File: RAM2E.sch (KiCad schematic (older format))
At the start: 19 parts, among them J1 AppleIIeAux, U1 EPM7128SL84, U2 2M x 8

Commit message: halfway done widening clearances
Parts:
- removed U2: 2M x 8, stdpads:SOJ-28-300mil, symbol Connector_Generic:Conn_02x14_Counter_Clockwise
- added C9: 10p, stdpads:C_0805, symbol Device:C_Small
- added R1: 820, stdpads:R_0805, symbol Device:R_Small
- added U2: DRAM_2Mx8, stdpads:SOJ-28-300mil, symbol stdparts:DRAM_2Mx8
- FID1, FID2, FID3, FID4: symbol Mechanical:MountingHole -> Mechanical:Fiducial
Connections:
- wire segments 260 -> 265
- no-connect marks 4 -> 5
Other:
- note added: "= don’t care"
- note added: "State = { PHI0, C7M, nPRAS, nPCAS, Q3 }\nGateCRAS <= state == 10100 | 01111 | 00011 | 01011 @ C14M↑\nnRefRAS <= ~state == 01111 | 01011 | 00001~ @ C14M↑\nnRefCAS <= ~state == 01111 | 00011~ @ C14M↓\nGateWE <= state == 10100 | 00011 @ C14M↑\nHoldRow <= state == 01011 | 10011 @ C14M↓\n\nRowAddr[7:0] <= MA[7:0] @ nPRAS↓\nBA[5:0] <= (state==10100 & RowAddr==73 & C07X) ? D[5:0] : BA[5:0] @ C14M↑"
- note added: "nRAS <= GateCRAS ? nRefRAS : nPRAS\nnCAS <= GateCRAS ? nRefCAS : Q3\nnRWE <= GateWE | RW80\nRA[7:0] <= HoldRow ? RowAddr[7:0] : MA[7:0]\nRA[10:8] <= PHI1 ? 0 : HoldRow ? BA[5:3] : BA[2:0]\nRA[11] <= PHI1 ? 0 : BA[5]\n\nVDR[7:0] <= RD[7:0] @ PHI0\nVD[7:0] <= PHI1 ? 8’bZ : VDR[7:0]\nD[7:0] <= (EN80 & R~W~80) ? RD[7:0] : 8’bZ\nRD[7:0] <= (EN80 & ~R~W80) ? D[7:0] : 8’bZ"
- note removed: "GateCRAS <= state == 10100 | 01111 | 00011 | 01011 @ C14M\nnRefRAS <= ~state == 01111 | 01011 | 00001~ @ C14M\nnRefCAS <= ~state == 01111 | 00011~ @ ~C14M~\nGateWE <= state == 10100 | 00011 @ C14M\nHoldRow <= state == 01011 | 10011 @ ~C14M~\n\nRowAddr[7:0] <= MA[7:0] @ ~nPRAS~\nBA[5:0] <= D[5:0] @ C14M in state == 10100 & RowAddr == 73 & C07X"
- note removed: "VDR[7:0] <= RD[7:0] @ PHI0\nVD[7:0] <= PHI1 ? 8’bZ : VDR[7:0]\nD[7:0] <= (EN80 & R~W~80) ? RD[7:0] : 8’bZ\nRD[7:0] <= (EN80 & ~R~W80) ? D[7:0] : 8’bZ"
- note removed: "nRAS <= GateCRAS ? nRefRAS : nPRAS\nnCAS <= GateCRAS ? nRefCAS : Q3\nnRWE <= GateWE | RW80\nRA[7:0] <= HoldRow ? RowAddr[7:0] : MA[7:0]\nRA[10:8] <= PHI1 ? 0 : HoldRow ? BA[5:3] : BA[2:0]\nRA[11] <= PHI1 ? 0 : BA[5]"
- moved on the sheet: C1, C2, C3, C4, C5, C6, C7, C8, H1, H2, H3, H4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

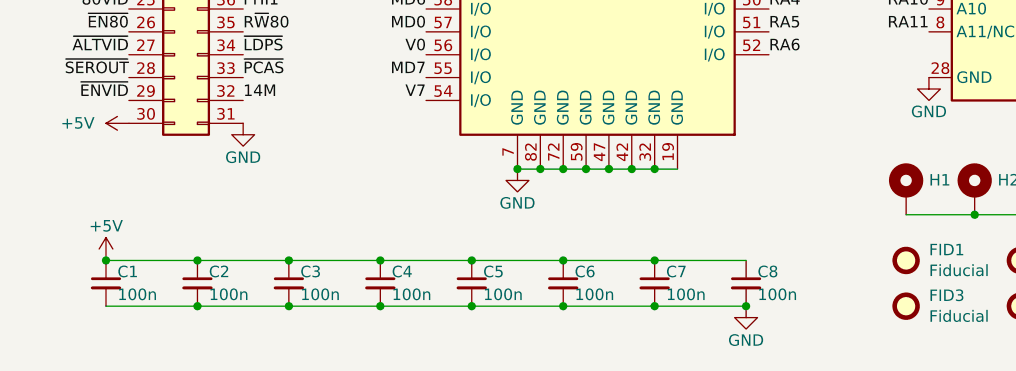
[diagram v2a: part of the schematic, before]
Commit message: Finished new revision 0.6
Wider clearance and 1 more bypass cap
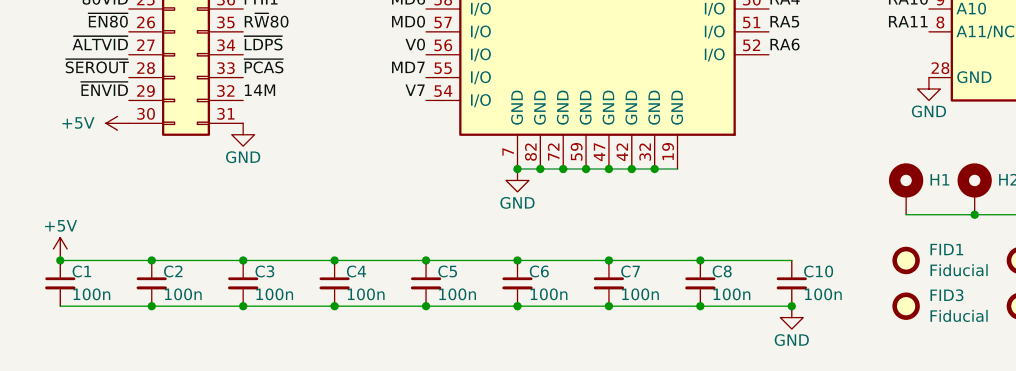
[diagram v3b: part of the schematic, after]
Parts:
- added C10: 100n, stdpads:C_0805, symbol Device:C_Small
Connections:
- wire segments 265 -> 267
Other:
- moved on the sheet: C1, C2, C3, C4, C5, C6, C7, C8
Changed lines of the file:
@@
 EESchema Schematic File Version 4
+LIBS:RAM2E-cache
 EELAYER 29 0
 EELAYER END
@@
 Title "RAM2E"
 Date "2019-07-15"
-Rev "0.5"
+Rev "0.6"
 Comp "Garrett's Workshop"
 Comment1 ""
@@
 L Device:C_Small C4
 U 1 1 5C4F04D1
-P 2300 7500
-F 0 "C4" H 2350 7550 50  0000 L CNN
-F 1 "100n" H 2350 7450 50  0000 L CNN
-F 2 "stdpads:C_0805" H 2300 7500 50  0001 C CNN
-F 3 "~" H 2300 7500 50  0001 C CNN
-	1    2300 7500
+P 2100 7500
+F 0 "C4" H 2150 7550 50  0000 L CNN
+F 1 "100n" H 2150 7450 50  0000 L CNN
+F 2 "stdpads:C_0805" H 2100 7500 50  0001 C CNN
+F 3 "~" H 2100 7500 50  0001 C CNN
+	1    2100 7500
 	1    0    0    -1
 $EndComp
@@
 L Device:C_Small C5
 U 1 1 5CB37AA0
-P 2700 7500
-F 0 "C5" H 2750 7550 50  0000 L CNN
-F 1 "100n" H 2750 7450 50  0000 L CNN
-F 2 "stdpads:C_0805" H 2700 7500 50  0001 C CNN
-F 3 "~" H 2700 7500 50  0001 C CNN
-	1    2700 7500
+P 2500 7500
+F 0 "C5" H 2550 7550 50  0000 L CNN
+F 1 "100n" H 2550 7450 50  0000 L CNN
+F 2 "stdpads:C_0805" H 2500 7500 50  0001 C CNN
+F 3 "~" H 2500 7500 50  0001 C CNN
+	1    2500 7500
 	1    0    0    -1
 $EndComp
@@
 L Device:C_Small C7
 U 1 1 5CB37AAE
-P 3500 7500
-F 0 "C7" H 3550 7550 50  0000 L CNN
-F 1 "100n" H 3550 7450 50  0000 L CNN
-F 2 "stdpads:C_0805" H 3500 7500 50  0001 C CNN
-F 3 "~" H 3500 7500 50  0001 C CNN
-	1    3500 7500
-	1    0    0    -1
-$EndComp
-Wire Wire Line
-	2700 7400 3100 7400
-Wire Wire Line
-	3500 7400 3900 7400
-Wire Wire Line
-	3900 7600 3500 7600
-Wire Wire Line
-	3100 7600 2700 7600
-Connection ~ 2700 7400
-Connection ~ 2700 7600
+P 3300 7500
+F 0 "C7" H 3350 7550 50  0000 L CNN
+F 1 "100n" H 3350 7450 50  0000 L CNN
+F 2 "stdpads:C_0805" H 3300 7500 50  0001 C CNN
+F 3 "~" H 3300 7500 50  0001 C CNN
+	1    3300 7500
+	1    0    0    -1
+$EndComp
+Wire Wire Line
+	2500 7400 2900 7400
+Wire Wire Line
+	3300 7400 3700 7400
+Wire Wire Line
+	3700 7600 3300 7600
+Wire Wire Line
+	2900 7600 2500 7600
+Connection ~ 2500 7400
+Connection ~ 2500 7600
 $Comp
 L Device:C_Small C8
 U 1 1 5CC13922
-P 3900 7500
-F 0 "C8" H 3950 7550 50  0000 L CNN
-F 1 "100n" H 3950 7450 50  0000 L CNN
-F 2 "stdpads:C_0805" H 3900 7500 50  0001 C CNN
-F 3 "~" H 3900 7500 50  0001 C CNN
-	1    3900 7500
+P 3700 7500
+F 0 "C8" H 3750 7550 50  0000 L CNN
+F 1 "100n" H 3750 7450 50  0000 L CNN
+F 2 "stdpads:C_0805" H 3700 7500 50  0001 C CNN
+F 3 "~" H 3700 7500 50  0001 C CNN
+	1    3700 7500
 	1    0    0    -1
 $EndComp
@@
 L Device:C_Small C6
 U 1 1 5D140E8E
-P 3100 7500
-F 0 "C6" H 3150 7550 50  0000 L CNN
-F 1 "100n" H 3150 7450 50  0000 L CNN
-F 2 "stdpads:C_0805" H 3100 7500 50  0001 C CNN
-F 3 "~" H 3100 7500 50  0001 C CNN
-	1    3100 7500
-	1    0    0    -1
-$EndComp
-Wire Wire Line
-	1500 7400 1900 7400
-Wire Wire Line
-	1500 7600 1900 7600
+P 2900 7500
+F 0 "C6" H 2950 7550 50  0000 L CNN
+F 1 "100n" H 2950 7450 50  0000 L CNN
+F 2 "stdpads:C_0805" H 2900 7500 50  0001 C CNN
+F 3 "~" H 2900 7500 50  0001 C CNN
+	1    2900 7500
+	1    0    0    -1
+$EndComp
+Wire Wire Line
+	1300 7400 1700 7400
+Wire Wire Line
+	1300 7600 1700 7600
 $Comp
 L Device:C_Small C3
 U 1 1 5D14D1AA
-P 1900 7500
-F 0 "C3" H 1950 7550 50  0000 L CNN
-F 1 "100n" H 1950 7450 50  0000 L CNN
-F 2 "stdpads:C_0805" H 1900 7500 50  0001 C CNN
-F 3 "~" H 1900 7500 50  0001 C CNN
-	1    1900 7500
+P 1700 7500
+F 0 "C3" H 1750 7550 50  0000 L CNN
+F 1 "100n" H 1750 7450 50  0000 L CNN
+F 2 "stdpads:C_0805" H 1700 7500 50  0001 C CNN
+F 3 "~" H 1700 7500 50  0001 C CNN
+	1    1700 7500
 	1    0    0    -1
 $EndComp
@@
 L Device:C_Small C2
 U 1 1 5D14D1B0
-P 1500 7500
-F 0 "C2" H 1550 7550 50  0000 L CNN
-F 1 "100n" H 1550 7450 50  0000 L CNN
-F 2 "stdpads:C_0805" H 1500 7500 50  0001 C CNN
-F 3 "~" H 1500 7500 50  0001 C CNN
-	1    1500 7500
-	1    0    0    -1
-$EndComp
-Wire Wire Line
-	1100 7600 1500 7600
-Wire Wire Line
-	1500 7400 1100 7400
-Connection ~ 1900 7400
-Wire Wire Line
-	1900 7400 2300 7400
-Connection ~ 1900 7600
-Wire Wire Line
-	1900 7600 2300 7600
-Connection ~ 2300 7400
-Wire Wire Line
-	2300 7400 2700 7400
-Connection ~ 2300 7600
-Wire Wire Line
-	2300 7600 2700 7600
+P 1300 7500
+F 0 "C2" H 1350 7550 50  0000 L CNN
+F 1 "100n" H 1350 7450 50  0000 L CNN
+F 2 "stdpads:C_0805" H 1300 7500 50  0001 C CNN
+F 3 "~" H 1300 7500 50  0001 C CNN
+	1    1300 7500
+	1    0    0    -1
+$EndComp
+Wire Wire Line
+	900  7600 1300 7600
+Wire Wire Line
+	1300 7400 900  7400
+Connection ~ 1700 7400
+Wire Wire Line
+	1700 7400 2100 7400
+Connection ~ 1700 7600
+Wire Wire Line
+	1700 7600 2100 7600
+Connection ~ 2100 7400
+Wire Wire Line
+	2100 7400 2500 7400
+Connection ~ 2100 7600
+Wire Wire Line
+	2100 7600 2500 7600
 $Comp
 L power:GND #PWR0105
 U 1 1 5D1550D4
-P 3900 7600
-F 0 "#PWR0105" H 3900 7350 50  0001 C CNN
-F 1 "GND" H 3900 7450 50  0000 C CNN
-F 2 "" H 3900 7600 50  0001 C CNN
-F 3 "" H 3900 7600 50  0001 C CNN
-	1    3900 7600
-	1    0    0    -1
-$EndComp
-Connection ~ 1500 7400
-Connection ~ 1500 7600
-Wire Wire Line
-	3100 7400 3500 7400
-Connection ~ 3100 7400
-Connection ~ 3500 7400
-Wire Wire Line
-	3100 7600 3500 7600
-Connection ~ 3500 7600
-Connection ~ 3100 7600
-Connection ~ 3900 7600
-Connection ~ 1100 7400
+P 4100 7600
+F 0 "#PWR0105" H 4100 7350 50  0001 C CNN
+F 1 "GND" H 4100 7450 50  0000 C CNN
+F 2 "" H 4100 7600 50  0001 C CNN
+F 3 "" H 4100 7600 50  0001 C CNN
+	1    4100 7600
+	1    0    0    -1
+$EndComp
+Connection ~ 1300 7400
+Connection ~ 1300 7600
+Wire Wire Line
+	2900 7400 3300 7400
+Connection ~ 2900 7400
+Connection ~ 3300 7400
+Wire Wire Line
+	2900 7600 3300 7600
+Connection ~ 3300 7600
+Connection ~ 2900 7600
+Connection ~ 900  7400
 $Comp
 L power:+5V #PWR0120
 U 1 1 5C293BD7
-P 1100 7400
-F 0 "#PWR0120" H 1100 7250 50  0001 C CNN
-F 1 "+5V" H 1100 7550 50  0000 C CNN
-F 2 "" H 1100 7400 50  0001 C CNN
-F 3 "" H 1100 7400 50  0001 C CNN
-	1    1100 7400
+P 900 7400
+F 0 "#PWR0120" H 900 7250 50  0001 C CNN
+F 1 "+5V" H 900 7550 50  0000 C CNN
+F 2 "" H 900 7400 50  0001 C CNN
+F 3 "" H 900 7400 50  0001 C CNN
+	1    900  7400
 	1    0    0    -1
 $EndComp
@@
 L Device:C_Small C1
 U 1 1 5D136B08
-P 1100 7500
-F 0 "C1" H 1150 7550 50  0000 L CNN
-F 1 "100n" H 1150 7450 50  0000 L CNN
-F 2 "stdpads:C_0805" H 1100 7500 50  0001 C CNN
-F 3 "~" H 1100 7500 50  0001 C CNN
-	1    1100 7500
+P 900 7500
+F 0 "C1" H 950 7550 50  0000 L CNN
+F 1 "100n" H 950 7450 50  0000 L CNN
+F 2 "stdpads:C_0805" H 900 7500 50  0001 C CNN
+F 3 "~" H 900 7500 50  0001 C CNN
+	1    900  7500
 	1    0    0    -1
 $EndComp
@@
 	1    0    0    -1
 $EndComp
+Text Label 4000 6500 0    50   ~ 0
+RA6
+$Comp
+L stdparts:DRAM_2Mx8 U2
+U 1 1 5DA22C4C
+P 5100 5900
+F 0 "U2" H 5100 6767 50  0000 C CNN
+F 1 "DRAM_2Mx8" H 5100 6676 50  0000 C CNN
+F 2 "stdpads:SOJ-28-300mil" H 5100 5050 50  0001 C CNN
+F 3 "https://www.alliancememory.com/wp-content/uploads/pdf/AS6C8008.pdf" H 5100 5350 50  0001 C CNN
+	1    5100 5900
+	1    0    0    -1
+$EndComp
+Wire Wire Line
+	5600 3050 5900 3050
+Wire Wire Line
+	5900 3050 5900 2950
+Wire Wire Line
+	5900 2950 6650 2950
+$Comp
+L Device:C_Small C10
+U 1 1 5D463FD5
+P 4100 7500
+F 0 "C10" H 4150 7550 50  0000 L CNN
+F 1 "100n" H 4150 7450 50  0000 L CNN
+F 2 "stdpads:C_0805" H 4100 7500 50  0001 C CNN
+F 3 "~" H 4100 7500 50  0001 C CNN
+	1    4100 7500
+	1    0    0    -1
+$EndComp
+Wire Wire Line
+	4100 7400 3700 7400
+Connection ~ 3700 7400
+Wire Wire Line
+	3700 7600 4100 7600
+Connection ~ 3700 7600
+Connection ~ 4100 7600
 $Comp
 L Device:C_Small C9
@@
 	-1   0    0    -1
 $EndComp
-Text Label 4000 6500 0    50   ~ 0
-RA6
-$Comp
-L stdparts:DRAM_2Mx8 U2
-U 1 1 5DA22C4C
-P 5100 5900
-F 0 "U2" H 5100 6767 50  0000 C CNN
-F 1 "DRAM_2Mx8" H 5100 6676 50  0000 C CNN
-F 2 "stdpads:SOJ-28-300mil" H 5100 5050 50  0001 C CNN
-F 3 "https://www.alliancememory.com/wp-content/uploads/pdf/AS6C8008.pdf" H 5100 5350 50  0001 C CNN
-	1    5100 5900
-	1    0    0    -1
-$EndComp
-Wire Wire Line
-	5600 3050 5900 3050
-Wire Wire Line
-	5900 3050 5900 2950
-Wire Wire Line
-	5900 2950 6650 2950
 $EndSCHEMATC

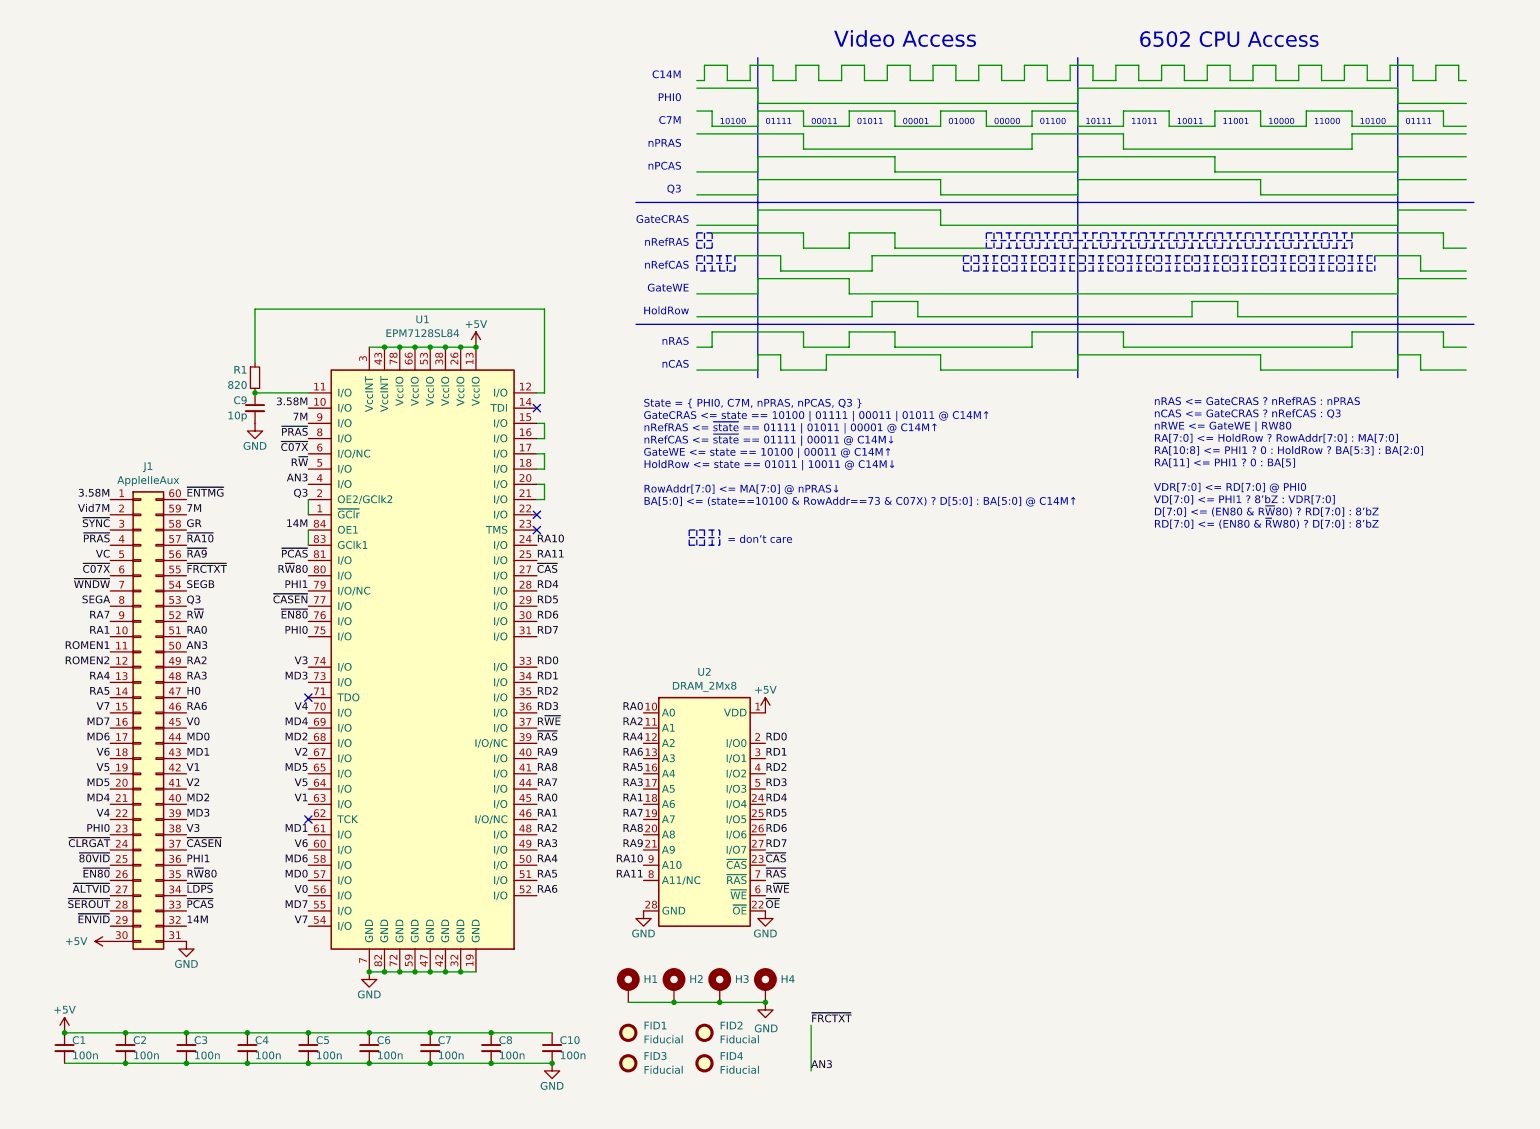
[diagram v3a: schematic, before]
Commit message: New CPLD idea
Also changed to 1k2R + 10pF RC delay
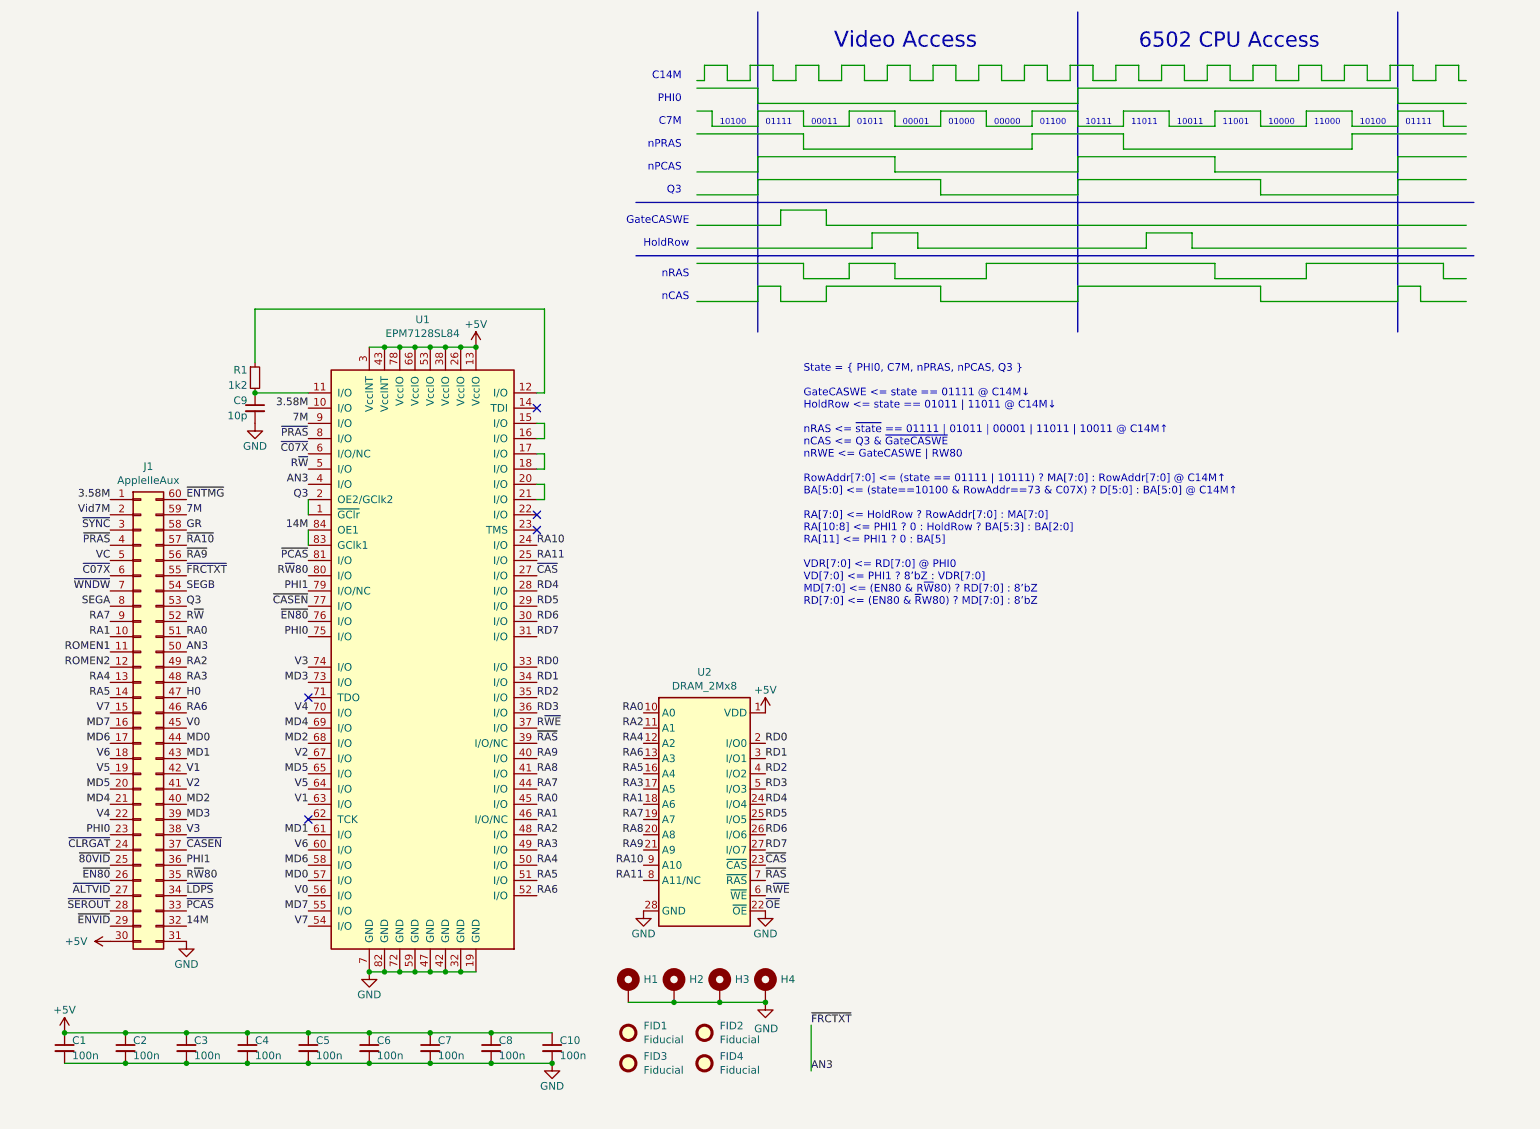
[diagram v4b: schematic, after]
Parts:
- R1: value 820 -> 1k2
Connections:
- wire segments 267 -> 238
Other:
- note added: "GateCASWE"
- note added: "State = { PHI0, C7M, nPRAS, nPCAS, Q3 }\n\nGateCASWE <= state == 01111 @ C14M↓\nHoldRow <= state == 01011 | 11011 @ C14M↓\n\nnRAS <= ~state == 01111 | 01011 | 00001 | 11011 | 10011~ @ C14M↑\nnCAS <= Q3 & ~GateCASWE~\nnRWE <= GateCASWE | RW80\n\nRowAddr[7:0] <= (state == 01111 | 10111) ? MA[7:0] : RowAddr[7:0] @ C14M↑\nBA[5:0] <= (state==10100 & RowAddr==73 & C07X) ? D[5:0] : BA[5:0] @ C14M↑\n\nRA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"
- note removed: "= don’t care"
- note removed: "GateCRAS"
- note removed: "GateWE"
- note removed: "State = { PHI0, C7M, nPRAS, nPCAS, Q3 }\nGateCRAS <= state == 10100 | 01111 | 00011 | 01011 @ C14M↑\nnRefRAS <= ~state == 01111 | 01011 | 00001~ @ C14M↑\nnRefCAS <= ~state == 01111 | 00011~ @ C14M↓\nGateWE <= state == 10100 | 00011 @ C14M↑\nHoldRow <= state == 01011 | 10011 @ C14M↓\n\nRowAddr[7:0] <= MA[7:0] @ nPRAS↓\nBA[5:0] <= (state==10100 & RowAddr==73 & C07X) ? D[5:0] : BA[5:0] @ C14M↑"
- note removed: "nRAS <= GateCRAS ? nRefRAS : nPRAS\nnCAS <= GateCRAS ? nRefCAS : Q3\nnRWE <= GateWE | RW80\nRA[7:0] <= HoldRow ? RowAddr[7:0] : MA[7:0]\nRA[10:8] <= PHI1 ? 0 : HoldRow ? BA[5:3] : BA[2:0]\nRA[11] <= PHI1 ? 0 : BA[5]\n\nVDR[7:0] <= RD[7:0] @ PHI0\nVD[7:0] <= PHI1 ? 8’bZ : VDR[7:0]\nD[7:0] <= (EN80 & R~W~80) ? RD[7:0] : 8’bZ\nRD[7:0] <= (EN80 & ~R~W80) ? D[7:0] : 8’bZ"
- note removed: "nRefCAS"
- note removed: "nRefRAS"

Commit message: Schematic documentation update
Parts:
- C1, C10, C2, C3, C4, C5, C6, C7, C8: value 100n -> 10u
- U1: symbol stdparts:EPM7128SL84 -> GW_PLD.lib:EPM7128SL84
- U2: symbol stdparts:DRAM_2Mx8 -> GW_RAM.lib:DRAM-2Mx8-SOP-28
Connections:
- net labels added: C14M, C3M58, C7M, MA0, MA1, MA2, MA3, MA4, MA5, MA6, MA7, VD0, VD1, VD2, VD3, VD4, VD5, VD6, VD7
- net labels removed: 14M, 3.58M, 7M, RA0, RA1, RA2, RA3, RA4, RA5, RA6, RA7, V0, V1, V2, V3, V4, V5, V6, V7
- wire segments 238 -> 131
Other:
- note added: "DelayIn/Out[0]"
- note added: "DelayIn/Out[1]"
- note added: "DelayIn/Out[2]"
- note added: "DelayIn/Out[3]"
- note removed: "00000"
- note removed: "00001"
- note removed: "00011"
- note removed: "01000"
- note removed: "01011"
- note removed: "01100"
- note removed: "01111"
- note removed: "10000"
- note removed: "10011"
- note removed: "10100"
- note removed: "10111"
- note removed: "11000"
- note removed: "11001"
- note removed: "11011"
- note removed: "6502 CPU Access"
- note removed: "C14M"
- note removed: "C7M"
- note removed: "GateCASWE"
- note removed: "HoldRow"
- note removed: "PHI0"
- note removed: "Q3"
- note removed: "State = { PHI0, C7M, nPRAS, nPCAS, Q3 }\n\nGateCASWE <= state == 01111 @ C14M↓\nHoldRow <= state == 01011 | 11011 @ C14M↓\n\nnRAS <= ~state == 01111 | 01011 | 00001 | 11011 | 10011~ @ C14M↑\nnCAS <= Q3 & ~GateCASWE~\nnRWE <= GateCASWE | RW80\n\nRowAddr[7:0] <= (state == 01111 | 10111) ? MA[7:0] : RowAddr[7:0] @ C14M↑\nBA[5:0] <= (state==10100 & RowAddr==73 & C07X) ? D[5:0] : BA[5:0] @ C14M↑\n\nRA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"
- note removed: "Video Access"
- note removed: "nCAS"
- note removed: "nPCAS"
- note removed: "nPRAS"
- note removed: "nRAS"
- moved on the sheet: C9, J1, R1, U1, U2
